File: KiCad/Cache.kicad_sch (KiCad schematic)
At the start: 15 parts, among them U801 61C256-15, U802 61C1024-20, U803 61C1024-20, U804 61C1024-20, U805 61C1024-20, U806 61C256-15, U807 61C256-15, U808 61C256-15, U809 61C256-15, U810 74F08, U811 74F125

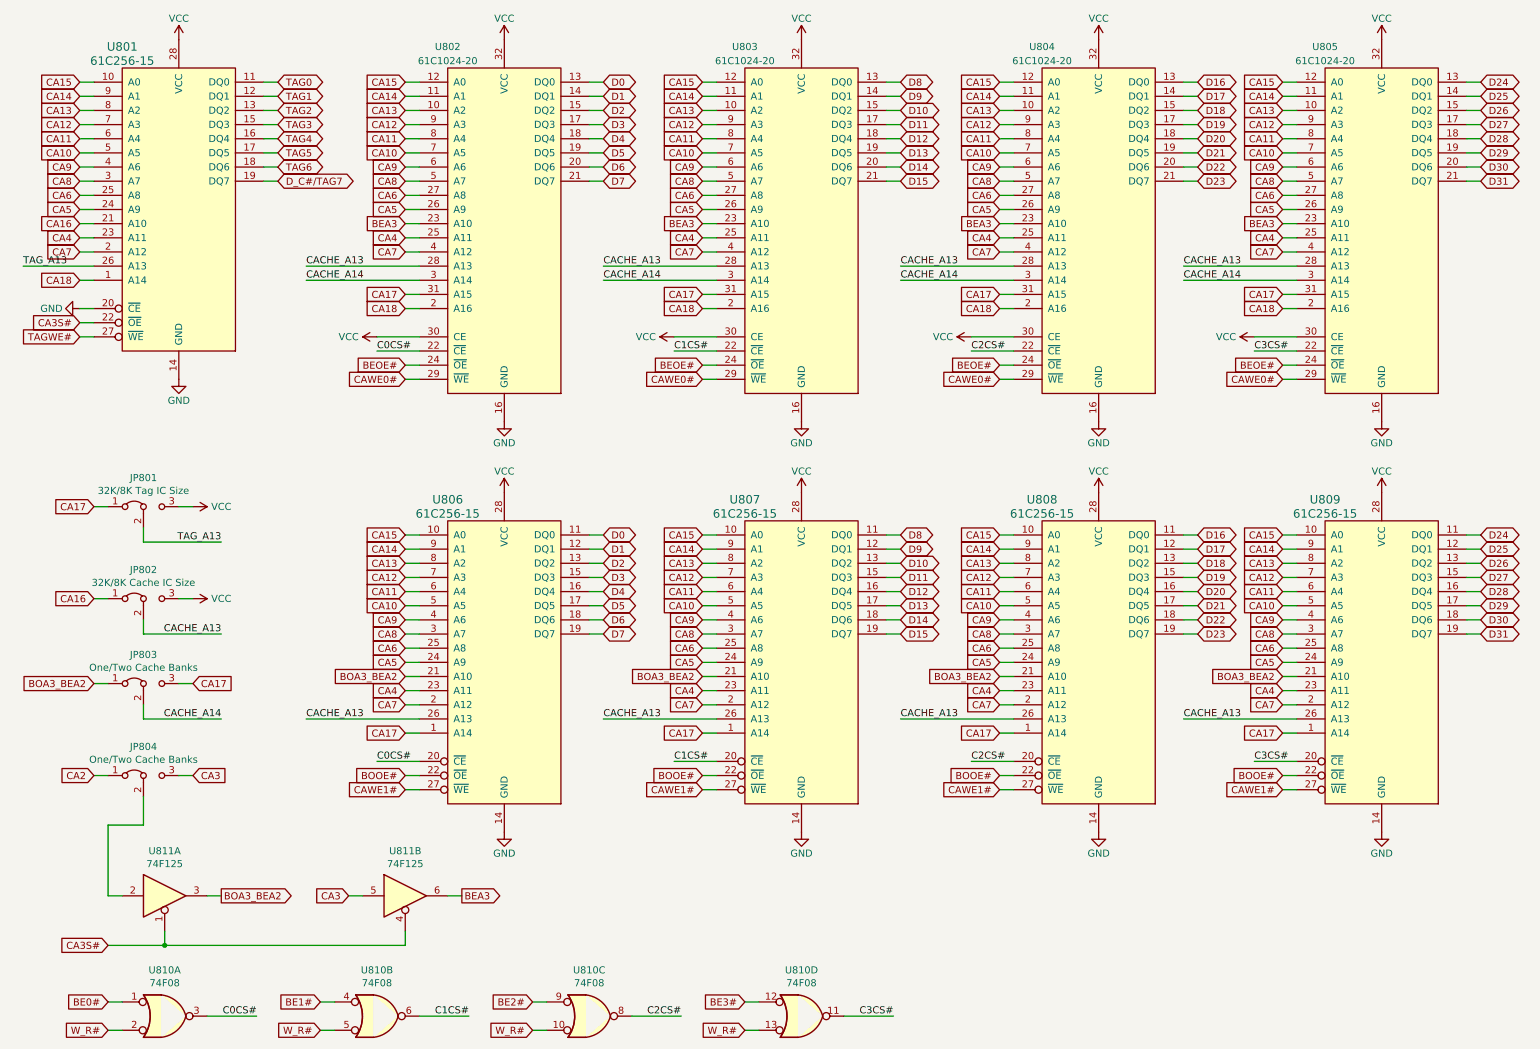
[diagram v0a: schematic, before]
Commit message: Version 0.2: Update cache schematic
Signed-off-by: Sergey Kiselev <sergey.kiselev@intel.com>
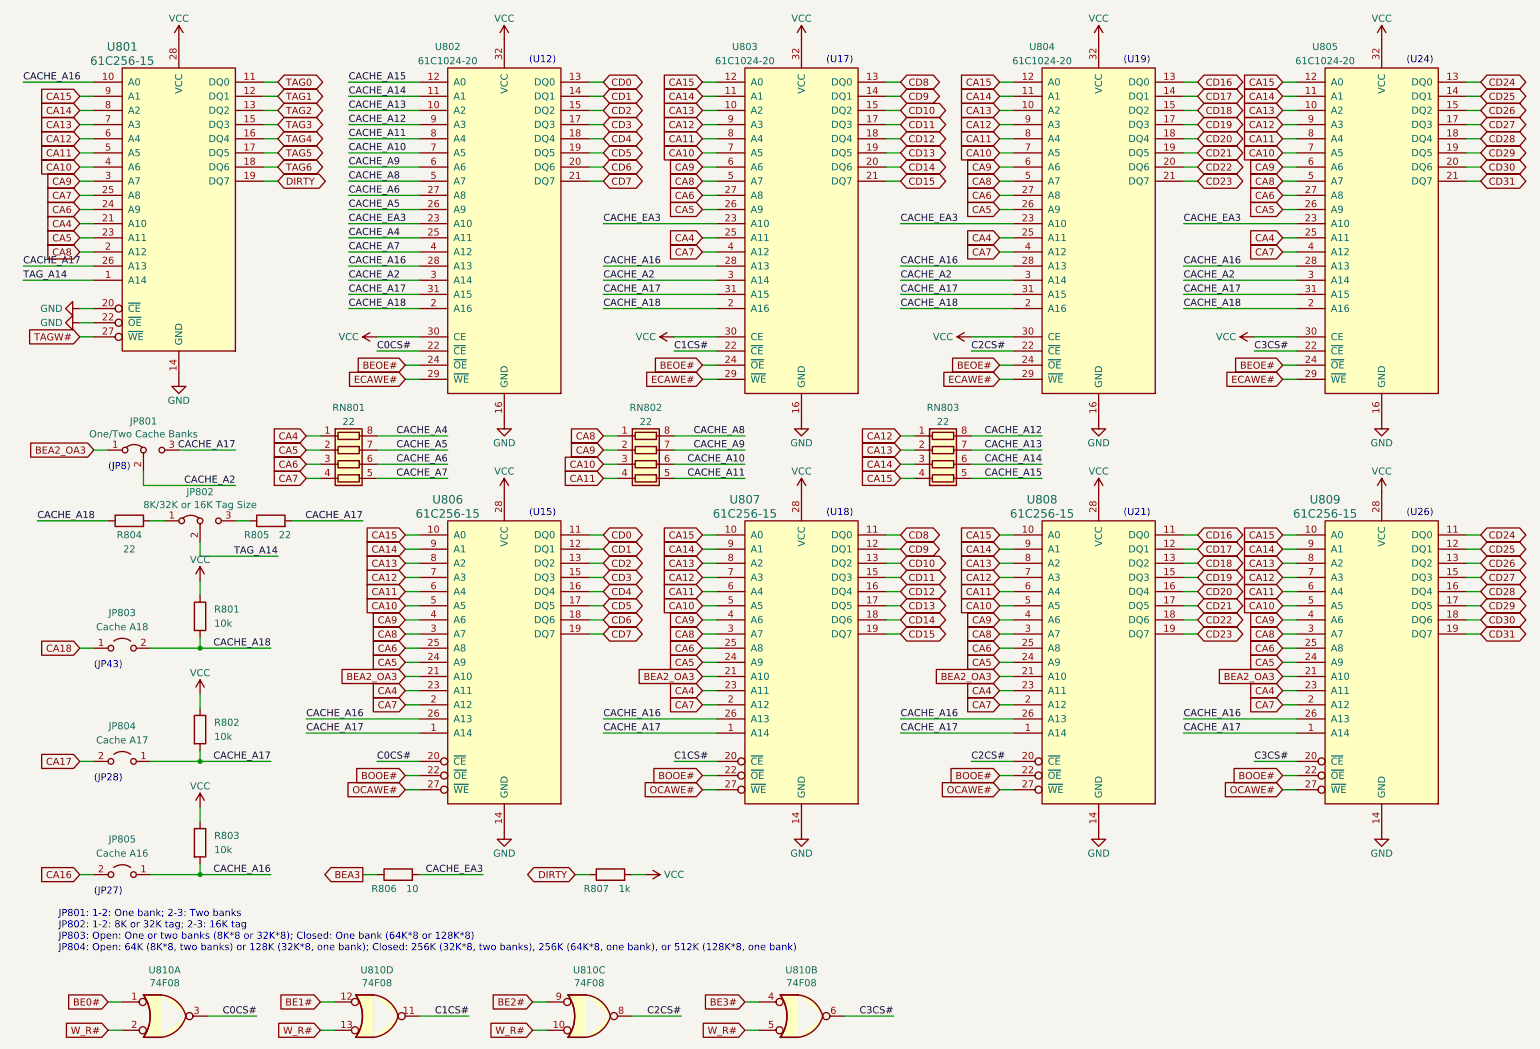
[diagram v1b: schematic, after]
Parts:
- removed JP801: 32K/8K Tag IC Size, symbol my_components:Jumper_3_Bridged12_Passive
- removed JP803: One/Two Cache Banks, symbol my_components:Jumper_3_Bridged12_Passive
- removed U811: 74F125, symbol 74xx:74LS125
- added JP803: Cache A18, symbol Jumper:Jumper_2_Open
- added JP804: Cache A17, symbol Jumper:Jumper_2_Open
- added JP805: Cache A16, symbol Jumper:Jumper_2_Open
- added R801, R802, R803: 10k, symbol Device:R
- added R804, R805: 22, symbol Device:R
- added R806: 10, symbol Device:R
- added R807: 1k, symbol Device:R
- added RN801, RN802, RN803: 22, symbol Device:R_Pack04
- JP802: value 32K/8K Cache IC Size -> 8K/32K or 16K Tag Size
- renumbered JP804 to JP801
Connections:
- net CA2 is gone; now on net BEA2_OA3: JP801.1 (A)
- net CA3S# is gone; now on net GND: U801.22 (~{OE})
- net TAG_A13 is gone; now on net CACHE_A17: U801.26 (A13)
- net BE1#: now also U810.12; no longer U810.4
- net BE3#: now also U810.4; no longer U810.12
- net BEA3: now also R806.1; no longer U802.23 (A10), U803.23 (A10), U804.23 (A10), U805.23 (A10)
- net C1CS#: now also U810.11; no longer U810.6
- net C3CS#: now also U810.6; no longer U810.11
- net CA10: now also U801.4 (A6), RN802.3 (R3.1); no longer U801.5 (A5), U802.7 (A5)
- net CA11: now also U801.5 (A5), RN802.4 (R4.1); no longer U801.6 (A4), U802.8 (A4)
- net CA12: now also U801.6 (A4), RN803.1 (R1.1); no longer U801.7 (A3), U802.9 (A3)
- net CA13: now also U801.7 (A3), RN803.2 (R2.1); no longer U801.8 (A2), U802.10 (A2)
- net CA14: now also U801.8 (A2), RN803.3 (R3.1); no longer U801.9 (A1), U802.11 (A1)
- net CA15: now also U801.9 (A1), RN803.4 (R4.1); no longer U801.10 (A0), U802.12 (A0)
- net CA16: now also JP805.2 (B); no longer JP802.1 (A), U801.21 (A10)
- net CA17: now also JP804.2 (B); no longer U802.31 (A15), U803.31 (A15), U804.31 (A15), U805.31 (A15), U806.1 (A14), U807.1 (A14), U808.1 (A14), U809.1 (A14)
- net CA18: now also JP803.1 (A); no longer U801.1 (A14), U802.2 (A16), U803.2 (A16), U804.2 (A16), U805.2 (A16)
- net CA4: now also U801.21 (A10), RN801.1 (R1.1); no longer U801.23 (A11), U802.25 (A11)
- net CA5: now also U801.23 (A11), RN801.2 (R2.1); no longer U801.24 (A9), U802.26 (A9)
- net CA6: now also U801.24 (A9), RN801.3 (R3.1); no longer U801.25 (A8), U802.27 (A8)
- net CA7: now also U801.25 (A8), RN801.4 (R4.1); no longer U801.2 (A12), U802.4 (A12)
- net CA8: now also U801.2 (A12), RN802.1 (R1.1); no longer U801.3 (A7), U802.5 (A7)
- net CA9: now also U801.3 (A7), RN802.2 (R2.1); no longer U801.4 (A6), U802.6 (A6)
- net CACHE_A13: now also U802.10 (A2), RN803.7 (R2.2); no longer JP802.2 (C), U802.28 (A13), U803.28 (A13), U804.28 (A13), U805.28 (A13), U806.26 (A13), U807.26 (A13), U808.26 (A13), U809.26 (A13)
- net CACHE_A14: now also U802.11 (A1), RN803.6 (R3.2); no longer U802.3 (A14), U803.3 (A14), U804.3 (A14), U805.3 (A14)
- net VCC: now also R801.1, R802.1, R803.1, R807.2; no longer JP802.3 (B)
- net CACHE_A2: now reaches JP801.2 (C)
- net CACHE_A2: now also U802.3 (A14), U803.3 (A14), U804.3 (A14), U805.3 (A14)
- net BOA3_BEA2 renamed BEA2_OA3
- net CA3 renamed CACHE_A17
- net CACHE_A17: now also U802.31 (A15), U803.31 (A15), U804.31 (A15), U805.31 (A15), U806.1 (A14), U807.1 (A14), U808.1 (A14), U809.1 (A14), JP804.1 (A), R802.2, R805.2
- net CAWE0# renamed ECAWE#
- net CAWE1# renamed OCAWE#
- net D0 renamed CD0
- net D1 renamed CD1
- net D10 renamed CD10
- net D11 renamed CD11
- net D12 renamed CD12
- net D13 renamed CD13
- net D14 renamed CD14
- net D15 renamed CD15
- net D16 renamed CD16
- net D17 renamed CD17
- net D18 renamed CD18
- net D19 renamed CD19
- net D2 renamed CD2
- net D20 renamed CD20
- net D21 renamed CD21
- net D22 renamed CD22
- net D23 renamed CD23
- net D24 renamed CD24
- net D25 renamed CD25
- net D26 renamed CD26
- net D27 renamed CD27
- net D28 renamed CD28
- net D29 renamed CD29
- net D3 renamed CD3
- net D30 renamed CD30
- net D31 renamed CD31
- net D4 renamed CD4
- net D5 renamed CD5
- net D6 renamed CD6
- net D7 renamed CD7
- net D8 renamed CD8
- net D9 renamed CD9
- net D_C#/TAG7 renamed DIRTY
- net DIRTY: now also R807.1
- net TAGWE# renamed TAGW#
- new net: JP802.1 (A), R804.2
- new net: JP802.3 (B), R805.1
- new net CACHE_A10: RN802.6 (R3.2), U802.7 (A5)
- new net CACHE_A11: RN802.5 (R4.2), U802.8 (A4)
- new net CACHE_A12: RN803.8 (R1.2), U802.9 (A3)
- new net CACHE_A15: RN803.5 (R4.2), U802.12 (A0)
- new net CACHE_A16: JP805.1 (A), R803.2, U801.10 (A0), U802.28 (A13), U803.28 (A13), U804.28 (A13), U805.28 (A13), U806.26 (A13), U807.26 (A13), U808.26 (A13), U809.26 (A13)
- new net CACHE_A18: JP803.2 (B), R801.2, R804.1, U802.2 (A16), U803.2 (A16), U804.2 (A16), U805.2 (A16)
- new net CACHE_A4: RN801.8 (R1.2), U802.25 (A11)
- new net CACHE_A5: RN801.7 (R2.2), U802.26 (A9)
- new net CACHE_A6: RN801.6 (R3.2), U802.27 (A8)
- new net CACHE_A7: RN801.5 (R4.2), U802.4 (A12)
- new net CACHE_A8: RN802.8 (R1.2), U802.5 (A7)
- new net CACHE_A9: RN802.7 (R2.2), U802.6 (A6)
- new net CACHE_EA3: R806.2, U802.23 (A10), U803.23 (A10), U804.23 (A10), U805.23 (A10)
- new net TAG_A14: JP802.2 (C), U801.1 (A14)
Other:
- note added: "(JP27)"
- note added: "(JP28)"
- note added: "(JP43)"
- note added: "(JP8)"
- note added: "(U12)"
- note added: "(U15)"
- note added: "(U17)"
- note added: "(U18)"
- note added: "(U19)"
- note added: "(U21)"
- note added: "(U24)"
- note added: "(U26)"
- note added: "JP801: 1-2: One bank; 2-3: Two banks JP802: 1-2: 8K or 32K tag; 2-3: 16K tag JP803: Open: One or two banks (8K*8 or 32K*8); Closed: One bank (64K*8 or 128K*8) JP804: Open: 64K (8K*8, two banks) or 128K (32K*8, one bank); Closed: 256K (32K*8, two banks), 256K (64K*8, one bank), or 512K (128K*8, one bank)"
- moved on the sheet: JP801, JP802, U810B, U810D

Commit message: Version 0.3: Update DRAM schematic, pull-ups/pull-downs, CPU configuration jumpers
Signed-off-by: Sergey Kiselev <skiselev@gmail.com>
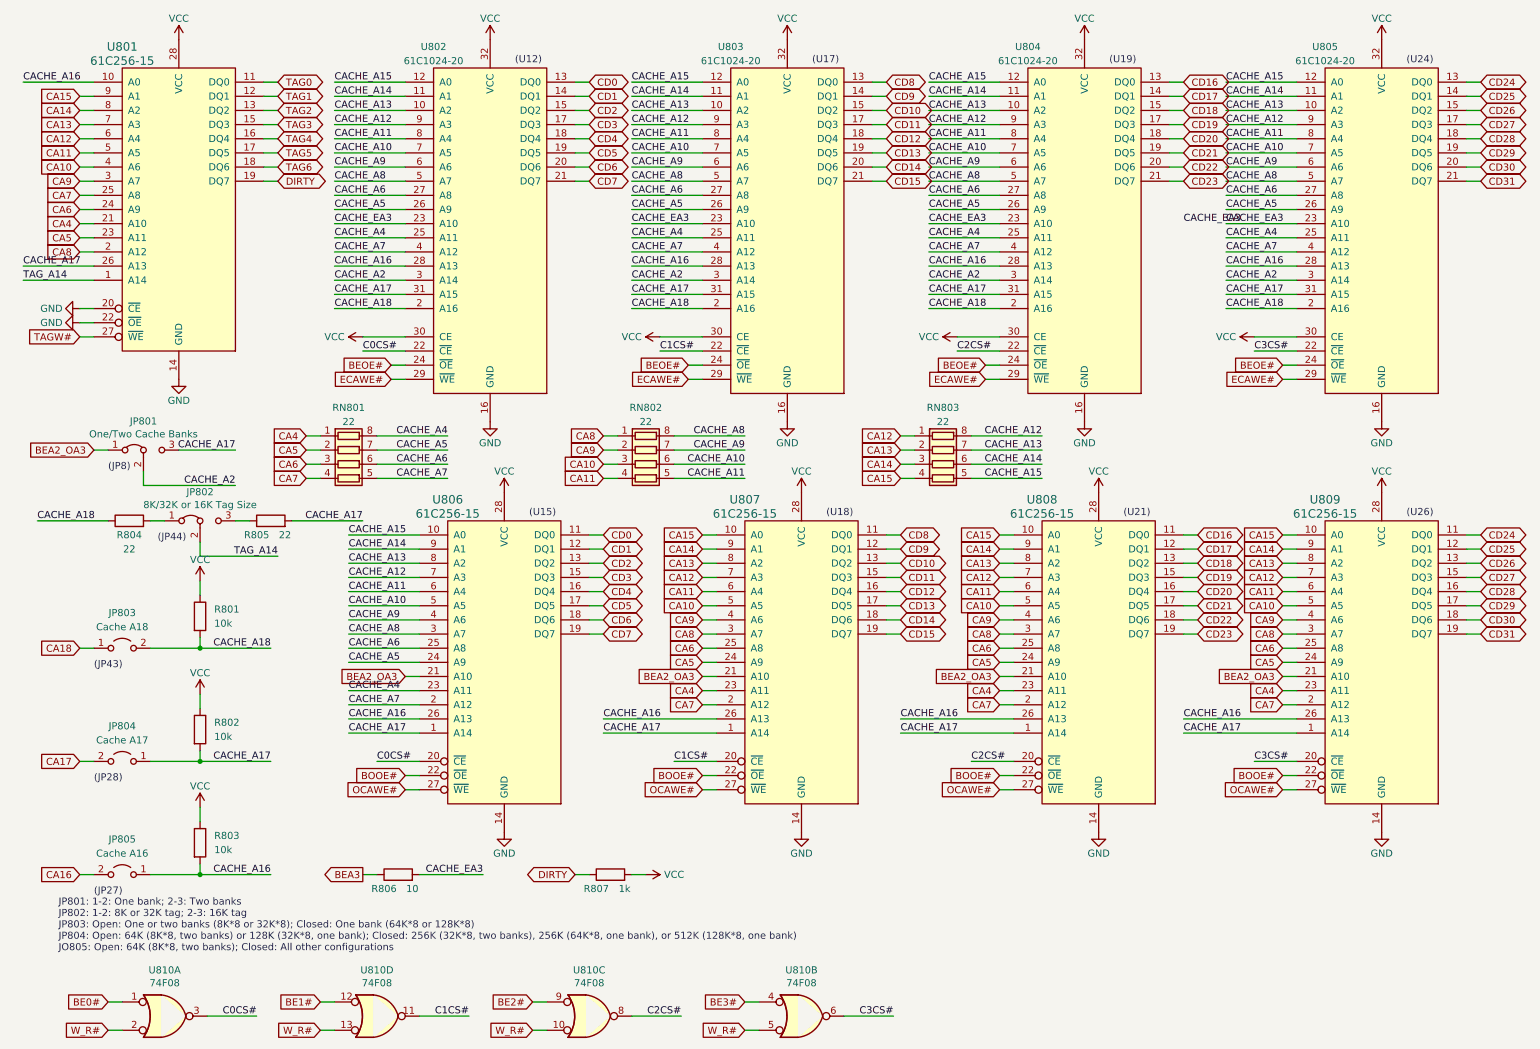
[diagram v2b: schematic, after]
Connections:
- net CA10: no longer U803.7 (A5), U804.7 (A5), U805.7 (A5), U806.5 (A5)
- net CA11: no longer U803.8 (A4), U804.8 (A4), U805.8 (A4), U806.6 (A4)
- net CA12: no longer U803.9 (A3), U804.9 (A3), U805.9 (A3), U806.7 (A3)
- net CA13: no longer U803.10 (A2), U804.10 (A2), U805.10 (A2), U806.8 (A2)
- net CA14: no longer U803.11 (A1), U804.11 (A1), U805.11 (A1), U806.9 (A1)
- net CA15: no longer U803.12 (A0), U804.12 (A0), U805.12 (A0), U806.10 (A0)
- net CA4: no longer U803.25 (A11), U804.25 (A11), U805.25 (A11), U806.23 (A11)
- net CA5: no longer U803.26 (A9), U804.26 (A9), U805.26 (A9), U806.24 (A9)
- net CA6: no longer U803.27 (A8), U804.27 (A8), U805.27 (A8), U806.25 (A8)
- net CA7: no longer U803.4 (A12), U804.4 (A12), U805.4 (A12), U806.2 (A12)
- net CA8: no longer U803.5 (A7), U804.5 (A7), U805.5 (A7), U806.3 (A7)
- net CA9: no longer U803.6 (A6), U804.6 (A6), U805.6 (A6), U806.4 (A6)
- net CACHE_A10: now also U803.7 (A5), U804.7 (A5), U805.7 (A5), U806.5 (A5)
- net CACHE_A11: now also U803.8 (A4), U804.8 (A4), U805.8 (A4), U806.6 (A4)
- net CACHE_A12: now also U803.9 (A3), U804.9 (A3), U805.9 (A3), U806.7 (A3)
- net CACHE_A13: now also U803.10 (A2), U804.10 (A2), U805.10 (A2), U806.8 (A2)
- net CACHE_A14: now also U803.11 (A1), U804.11 (A1), U805.11 (A1), U806.9 (A1)
- net CACHE_A15: now also U803.12 (A0), U804.12 (A0), U805.12 (A0), U806.10 (A0)
- net CACHE_A4: now also U803.25 (A11), U804.25 (A11), U805.25 (A11), U806.23 (A11)
- net CACHE_A5: now also U803.26 (A9), U804.26 (A9), U805.26 (A9), U806.24 (A9)
- net CACHE_A6: now also U803.27 (A8), U804.27 (A8), U805.27 (A8), U806.25 (A8)
- net CACHE_A7: now also U803.4 (A12), U804.4 (A12), U805.4 (A12), U806.2 (A12)
- net CACHE_A8: now also U803.5 (A7), U804.5 (A7), U805.5 (A7), U806.3 (A7)
- net CACHE_A9: now also U803.6 (A6), U804.6 (A6), U805.6 (A6), U806.4 (A6)
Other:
- note added: "(JP44)"
- note added: "JP801: 1-2: One bank; 2-3: Two banks JP802: 1-2: 8K or 32K tag; 2-3: 16K tag JP803: Open: One or two banks (8K*8 or 32K*8); Closed: One bank (64K*8 or 128K*8) JP804: Open: 64K (8K*8, two banks) or 128K (32K*8, one bank); Closed: 256K (32K*8, two banks), 256K (64K*8, one bank), or 512K (128K*8, one bank) JO805: Open: 64K (8K*8, two banks); Closed: All other configurations"
- note removed: "JP801: 1-2: One bank; 2-3: Two banks JP802: 1-2: 8K or 32K tag; 2-3: 16K tag JP803: Open: One or two banks (8K*8 or 32K*8); Closed: One bank (64K*8 or 128K*8) JP804: Open: 64K (8K*8, two banks) or 128K (32K*8, one bank); Closed: 256K (32K*8, two banks), 256K (64K*8, one bank), or 512K (128K*8, one bank)"
- moved on the sheet: U802, U803, U804
